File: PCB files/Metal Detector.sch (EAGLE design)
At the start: 14 parts, among them IC1 NE5534AD, Q1 IRF740, Q2 BC556, T1 BC547, X1 A1944-50

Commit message: Add files via upload
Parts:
- added C2, C3, C5: 0.1uF, SparkFun-Capacitors:0.1UF-0402-6.3V-10%-X7R
- added C4: 15pF, SparkFun-Capacitors:0.1UF-0402-6.3V-10%-X7R
- added C7: 10uF, SparkFun-Capacitors:10UF-0402T-6.3V-20%
- added D2, D3: 1N4148DO35-7, diode:1N4148DO35-7
- added R10: 1K, rcl:R-EU_0207/10
- added R8: 22K, rcl:R-EU_0207/10
- added R9: 1M, rcl:R-EU_0207/10
- added TR1: 1K, rcl:R-TRIMM3296X
- added TR2: 100K, rcl:R-TRIMM3296X
- R1: value (none) -> 10K
- R2: value (none) -> 1R
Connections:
- net PULSE renamed PULSE_PIN
- new net ADC_PIN: IC1.OUT, R9.2
- new net N$10: R8.1, TR2.S
- new net N$11: C5.2, IC1.ON/CMP, TR2.E
- new net N$12: C4.2, IC1.-IN, R10.2, R9.1
- new net N$13: C5.1, IC1.CMP
- new net N$9: IC1.ON, TR2.A
- net GND: now also C2.2, C3.2, C4.1, C7.1, D2.A, D3.C, R10.1, TR1.S
- net N$1: now also TR1.A
- net N$2: now also D2.C, D3.A
- net VCC: now also C2.1, C3.1, C7.2, IC1.V+, IC1.V-, R8.2
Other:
- moved on the sheet: C1, D1, IC1, Q1, Q2, R1, R2, R3, R4, R5, R6, R7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

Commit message: Add files via upload
Adding MCU sheet
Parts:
- added IC2: ESP32-WROOM-32UE-N4, ESP32-WROOM-32UE-N4:ESP32-WROOM-32UE-N4
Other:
- note added: "MCU (ESP32- ­WROOM­-32UE)"
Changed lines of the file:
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@@
 <grid distance="0.1" unitdist="inch" unit="inch" style="lines" multiple="1" display="no" altdistance="0.01" altunitdist="inch" altunit="inch"/>
 <layers>
-<layer number="1" name="Top" color="4" fill="1" visible="yes" active="no"/>
-<layer number="16" name="Bottom" color="1" fill="1" visible="yes" active="no"/>
-<layer number="17" name="Pads" color="2" fill="1" visible="yes" active="no"/>
-<layer number="18" name="Vias" color="2" fill="1" visible="yes" active="no"/>
-<layer number="19" name="Unrouted" color="6" fill="1" visible="yes" active="no"/>
-<layer number="20" name="Dimension" color="24" fill="1" visible="yes" active="no"/>
-<layer number="21" name="tPlace" color="16" fill="1" visible="yes" active="no"/>
-<layer number="22" name="bPlace" color="14" fill="1" visible="yes" active="no"/>
-<layer number="23" name="tOrigins" color="15" fill="1" visible="yes" active="no"/>
-<layer number="24" name="bOrigins" color="15" fill="1" visible="yes" active="no"/>
-<layer number="25" name="tNames" color="7" fill="1" visible="yes" active="no"/>
-<layer number="26" name="bNames" color="7" fill="1" visible="yes" active="no"/>
-<layer number="27" name="tValues" color="7" fill="1" visible="yes" active="no"/>
-<layer number="28" name="bValues" color="7" fill="1" visible="yes" active="no"/>
+<layer number="1" name="Top" color="4" fill="1" visible="no" active="no"/>
+<layer number="16" name="Bottom" color="1" fill="1" visible="no" active="no"/>
+<layer number="17" name="Pads" color="2" fill="1" visible="no" active="no"/>
+<layer number="18" name="Vias" color="2" fill="1" visible="no" active="no"/>
+<layer number="19" name="Unrouted" color="6" fill="1" visible="no" active="no"/>
+<layer number="20" name="Dimension" color="24" fill="1" visible="no" active="no"/>
+<layer number="21" name="tPlace" color="16" fill="1" visible="no" active="no"/>
+<layer number="22" name="bPlace" color="14" fill="1" visible="no" active="no"/>
+<layer number="23" name="tOrigins" color="15" fill="1" visible="no" active="no"/>
+<layer number="24" name="bOrigins" color="15" fill="1" visible="no" active="no"/>
+<layer number="25" name="tNames" color="7" fill="1" visible="no" active="no"/>
+<layer number="26" name="bNames" color="7" fill="1" visible="no" active="no"/>
+<layer number="27" name="tValues" color="7" fill="1" visible="no" active="no"/>
+<layer number="28" name="bValues" color="7" fill="1" visible="no" active="no"/>
 <layer number="29" name="tStop" color="15" fill="3" visible="no" active="no"/>
 <layer number="30" name="bStop" color="7" fill="6" visible="no" active="no"/>
@@
 <layer number="35" name="tGlue" color="7" fill="4" visible="no" active="no"/>
 <layer number="36" name="bGlue" color="7" fill="5" visible="no" active="no"/>
-<layer number="37" name="tTest" color="7" fill="1" visible="yes" active="no"/>
-<layer number="38" name="bTest" color="7" fill="1" visible="yes" active="no"/>
+<layer number="37" name="tTest" color="7" fill="1" visible="no" active="no"/>
+<layer number="38" name="bTest" color="7" fill="1" visible="no" active="no"/>
 <layer number="39" name="tKeepout" color="4" fill="11" visible="no" active="no"/>
 <layer number="40" name="bKeepout" color="1" fill="11" visible="no" active="no"/>
@@
 <layer number="44" name="Drills" color="7" fill="1" visible="no" active="no"/>
 <layer number="45" name="Holes" color="7" fill="1" visible="no" active="no"/>
-<layer number="46" name="Milling" color="3" fill="1" visible="yes" active="no"/>
-<layer number="47" name="Measures" color="7" fill="1" visible="yes" active="no"/>
-<layer number="48" name="Document" color="7" fill="1" visible="yes" active="no"/>
-<layer number="49" name="Reference" color="13" fill="1" visible="yes" active="no"/>
-<layer number="50" name="dxf" color="7" fill="1" visible="yes" active="no"/>
-<layer number="51" name="tDocu" color="6" fill="1" visible="yes" active="no"/>
-<layer number="52" name="bDocu" color="7" fill="1" visible="yes" active="no"/>
-<layer number="53" name="tGND_GNDA" color="7" fill="9" visible="yes" active="no"/>
-<layer number="54" name="bGND_GNDA" color="1" fill="9" visible="yes" active="no"/>
-<layer number="56" name="wert" color="7" fill="1" visible="yes" active="no"/>
-<layer number="57" name="tCAD" color="7" fill="1" visible="yes" active="no"/>
-<layer number="58" name="bCAD" color="7" fill="1" visible="yes" active="no"/>
-<layer number="59" name="tCarbon" color="7" fill="1" visible="yes" active="no"/>
-<layer number="60" name="bCarbon" color="7" fill="1" visible="yes" active="no"/>
+<layer number="46" name="Milling" color="3" fill="1" visible="no" active="no"/>
+<layer number="47" name="Measures" color="7" fill="1" visible="no" active="no"/>
+<layer number="48" name="Document" color="7" fill="1" visible="no" active="no"/>
+<layer number="49" name="Reference" color="13" fill="1" visible="no" active="no"/>
+<layer number="50" name="dxf" color="7" fill="1" visible="no" active="no"/>
+<layer number="51" name="tDocu" color="6" fill="1" visible="no" active="no"/>
+<layer number="52" name="bDocu" color="7" fill="1" visible="no" active="no"/>
+<layer number="53" name="tGND_GNDA" color="7" fill="9" visible="no" active="no"/>
+<layer number="54" name="bGND_GNDA" color="1" fill="9" visible="no" active="no"/>
+<layer number="56" name="wert" color="7" fill="1" visible="no" active="no"/>
+<layer number="57" name="tCAD" color="7" fill="1" visible="no" active="no"/>
+<layer number="58" name="bCAD" color="7" fill="1" visible="no" active="no"/>
+<layer number="59" name="tCarbon" color="7" fill="1" visible="no" active="no"/>
+<layer number="60" name="bCarbon" color="7" fill="1" visible="no" active="no"/>
 <layer number="88" name="SimResults" color="9" fill="1" visible="yes" active="yes"/>
 <layer number="89" name="SimProbes" color="9" fill="1" visible="yes" active="yes"/>
@@
 <part name="C7" library="SparkFun-Capacitors" library_urn="urn:adsk.eagle:library:510" deviceset="10UF" device="-0402T-6.3V-20%" package3d_urn="urn:adsk.eagle:package:41385069/1" value="10uF"/>
 <part name="SUPPLY7" library="supply2" library_urn="urn:adsk.eagle:library:372" deviceset="GND" device=""/>
+<part name="FRAME2" library="SparkFun-Aesthetics" library_urn="urn:adsk.eagle:library:507" deviceset="FRAME-A4L" device=""/>
+<part name="IC2" library="ESP32-WROOM-32UE-N4" deviceset="ESP32-WROOM-32UE-N4" device=""/>
 </parts>
 <sheets>
@@
 <sheet>
 <plain>
+<text x="-86.36" y="205.74" size="6.4516" layer="94">MCU (ESP32- ­WROOM­-32UE)</text>
 </plain>
 <instances>
+<instance part="FRAME2" gate="G$1" x="-165.1" y="43.18" smashed="yes">
+<attribute name="DRAWING_NAME" x="16.51" y="54.61" size="2.54" layer="94" font="vector"/>
+<attribute name="LAST_DATE_TIME" x="16.51" y="49.53" size="2.286" layer="94" font="vector"/>
+<attribute name="SHEET" x="30.48" y="44.45" size="2.54" layer="94" font="vector"/>
+<attribute name="DESIGNER" x="61.16" y="49.53" size="2.54" layer="94" font="vector"/>
+</instance>
+<instance part="IC2" gate="G$1" x="-5.08" y="172.72" smashed="yes">
+<attribute name="NAME" x="29.21" y="180.34" size="1.778" layer="95" align="center-left"/>
+<attribute name="VALUE" x="-1.27" y="109.22" size="1.778" layer="96" align="center-left"/>
+</instance>
 </instances>
 <busses>

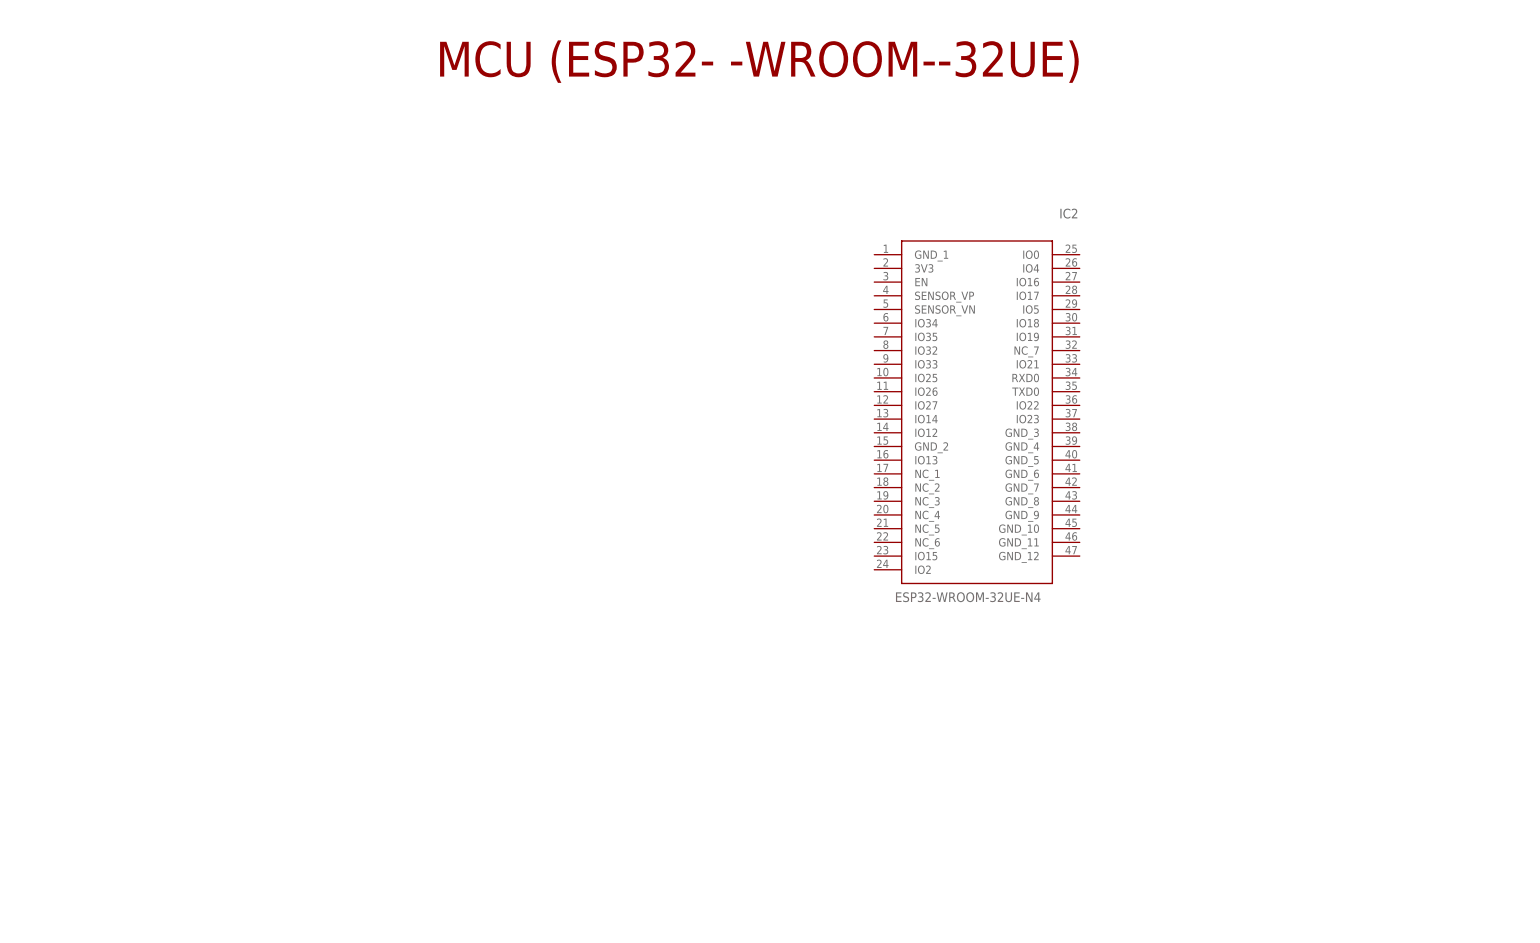
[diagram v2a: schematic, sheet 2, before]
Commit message: Add files via upload
Adding MCU peripherals, still designin MCU parts
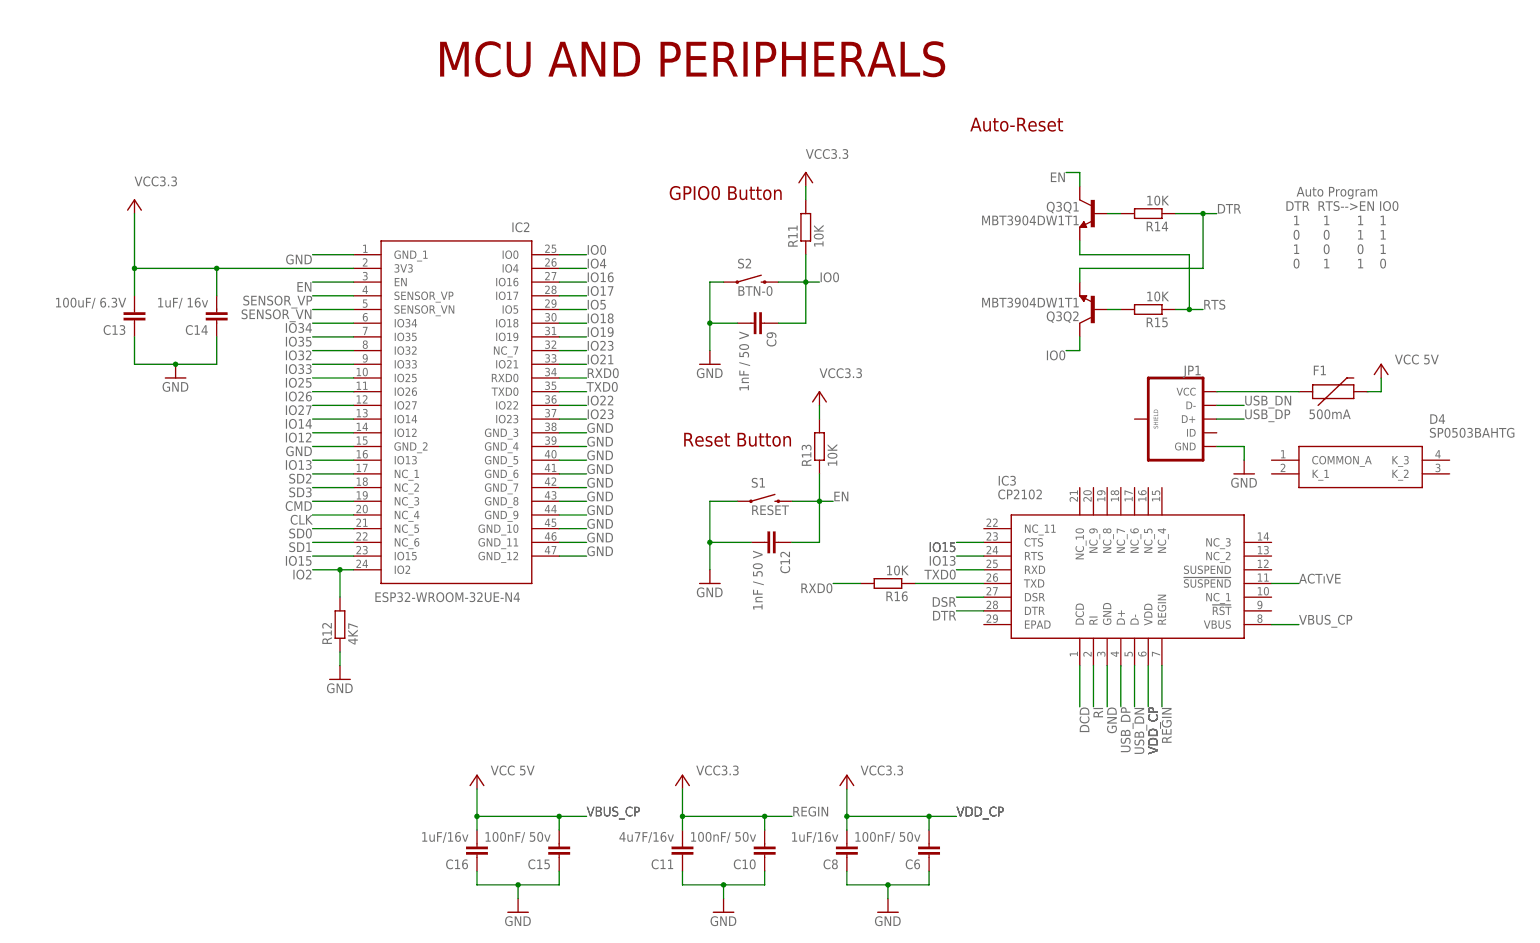
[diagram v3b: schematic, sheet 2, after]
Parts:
- added C10, C15, C6: 100nF/ 50v, rcl:C-EUC0603
- added C11: 4u7F/16v, rcl:C-EUC0603
- added C12, C9: 1nF / 50 V, rcl:C-EUC0603
- added C13: 100uF/ 6.3V, rcl:C-EUC0603
- added C14: 1uF/ 16v, rcl:C-EUC0603
- added C16, C8: 1uF/16v, rcl:C-EUC0603
- added D4: SP0503BAHTG, SP0503BAHTG:SP0503BAHTG
- added F1: 500mA, SparkFun-PowerIC:PTCSMD
- added IC3: CP2102, CP2102:CP2102
- added JP1: (no value), SparkFun-Connectors:USB_MICROB_PLUGCONN-11752
- added Q3: MBT3904DW1T1, esp32-thing-temp:MBT3904DW1T1
- added R11, R13, R14, R15, R16: 10K, rcl:R-EU_R0603
- added R12: 4K7, rcl:R-EU_R0603
- added S1: RESET, SparkFun-Electromechanical:SWITCH-MOMENTARY-2SMD-4.6X2.8MM
- added S2: BTN-0, SparkFun-Electromechanical:SWITCH-MOMENTARY-2SMD-4.6X2.8MM
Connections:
- new net ACTıVE: IC3.!SUSPEND
- new net CLK: IC2.NC_4
- new net CMD: IC2.NC_3
- new net DCD: IC3.DCD
- new net DSR: IC3.DSR
- new net DTR: IC3.DTR, Q3Q2.E, R14.1
- new net EN: C12.1, IC2.EN, Q3Q1.C, R13.1, S1.2
- new net IO0: C9.1, IC2.IO0, Q3Q2.C, R11.1, S2.2
- new net IO12: IC2.IO12
- new net IO13: IC2.IO13, IC3.RTS
- new net IO14: IC2.IO14
- new net IO15: IC2.IO15, IC3.CTS
- new net IO16: IC2.IO16
- new net IO17: IC2.IO17
- new net IO18: IC2.IO18
- new net IO19: IC2.IO19
- new net IO2: IC2.IO2, R12.2
- new net IO21: IC2.IO21
- new net IO22: IC2.IO22
- new net IO23: IC2.IO23, IC2.NC_7
- new net IO25: IC2.IO25
- new net IO26: IC2.IO26
- new net IO27: IC2.IO27
- new net IO32: IC2.IO32
- new net IO33: IC2.IO33
- new net IO34: IC2.IO34
- new net IO35: IC2.IO35
- new net IO4: IC2.IO4
- new net IO5: IC2.IO5
- new net N$14: Q3Q1.B, R14.2
- new net N$15: Q3Q2.B, R15.2
- new net N$16: IC3.TXD, R16.1
- new net N$17: F1.1, JP1.VCC
- new net REGIN: C10.2, C11.2, IC3.REGIN
- new net RI: IC3.RI
- new net RTS: Q3Q1.E, R15.1
- new net RXD0: IC2.RXD0, R16.2
- new net SD0: IC2.NC_5
- new net SD1: IC2.NC_6
- new net SD2: IC2.NC_1
- new net SD3: IC2.NC_2
- new net SENSOR_VN: IC2.SENSOR_VN
- new net SENSOR_VP: IC2.SENSOR_VP
- new net TXD0: IC2.TXD0, IC3.RXD
- new net USB_DN: IC3.D-, JP1.D-
- new net USB_DP: IC3.D+, JP1.D+
- new net VBUS_CP: C15.2, C16.2, IC3.VBUS
- new net VDD_CP: C6.2, C8.2, IC3.VDD
- net GND: now also C10.1, C11.1, C12.2, C13.1, C14.1, C15.1, C16.1, C6.1, C8.1, C9.2, IC2.GND_1, IC2.GND_10, IC2.GND_11, IC2.GND_12, IC2.GND_2, IC2.GND_3, IC2.GND_4, IC2.GND_5, IC2.GND_6, IC2.GND_7, IC2.GND_8, IC2.GND_9, IC3.GND, JP1.GND, R12.1, S1.1, S2.1
- net VCC: now also C13.2, C14.2, F1.2, IC2.3V3, R11.2, R13.2
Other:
- note added: "Auto Program DTR RTS-->EN IO0 1 1 1 1 0 0 1 1 1 0 0 1 0 1 1 0"
- note added: "Auto-Reset"
- note added: "GPIO0 Button"
- note added: "MCU AND PERIPHERALS"
- note added: "Reset Button"
- note removed: "MCU (ESP32- ­WROOM­-32UE)"
- moved on the sheet: IC2

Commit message: Add files via upload
Completed designing MCU and Peripheral sheet
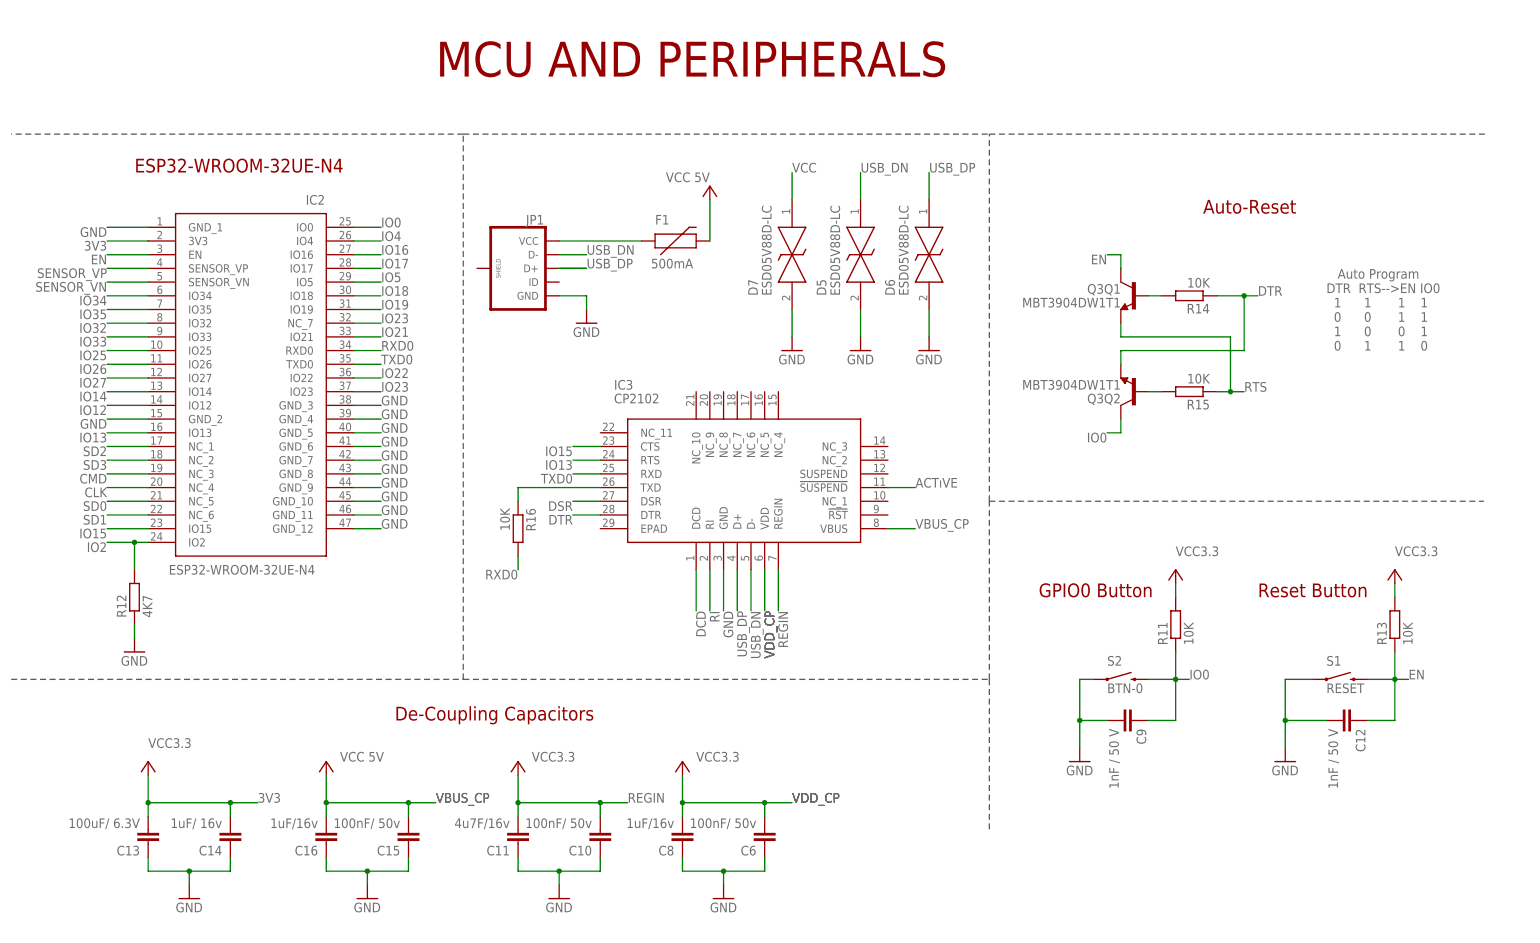
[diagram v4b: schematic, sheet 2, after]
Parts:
- removed D4: SP0503BAHTG, SP0503BAHTG:SP0503BAHTG
- added D5, D6, D7: ESD05V88D-LC, ESD05V88D-LC:ESD05V88D-LC
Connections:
- new net 3V3: C13.2, C14.2, IC2.3V3
- net GND: now also D5.2, D6.2, D7.2
- net USB_DN: now also D5.1
- net USB_DP: now also D6.1
- net VCC: now also D7.1; no longer C13.2, C14.2, IC2.3V3
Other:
- note added: "De-Coupling Capacitors"
- note added: "ESP32-WROOM-32UE-N4"
- moved on the sheet: C10, C11, C12, C13, C14, C15, C16, C6, C8, C9, F1, IC2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

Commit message: Add files via upload
Adding Subtitle to sheet
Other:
- note added: "USB to UART (Micro USB and CP2102)"
- moved on the sheet: D5, D6, D7, F1, IC3, JP1, Q3Q1, Q3Q2, R14, R15, R16
